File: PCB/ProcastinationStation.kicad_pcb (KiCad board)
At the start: 2 copper layers, 87 x 120 mm, 21 parts, among them J1 Conn_01x14_Socket, SW1 Up, SW10 X, SW11 L1, SW12 R2, SW13 Right, SW14 Y, SW2 A, SW3 Start, SW4 R1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

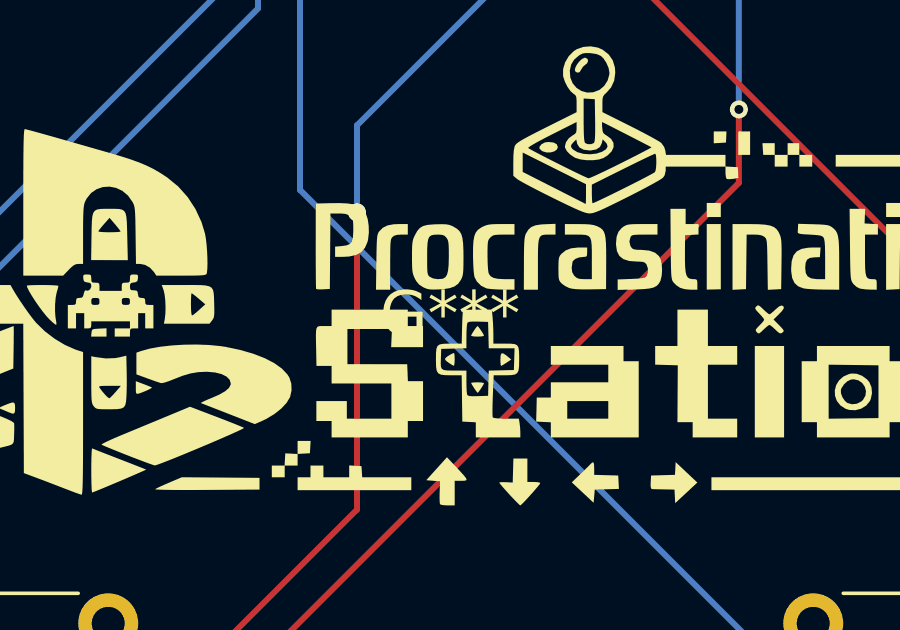
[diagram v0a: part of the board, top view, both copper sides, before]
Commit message: Update PCB schematic and layout
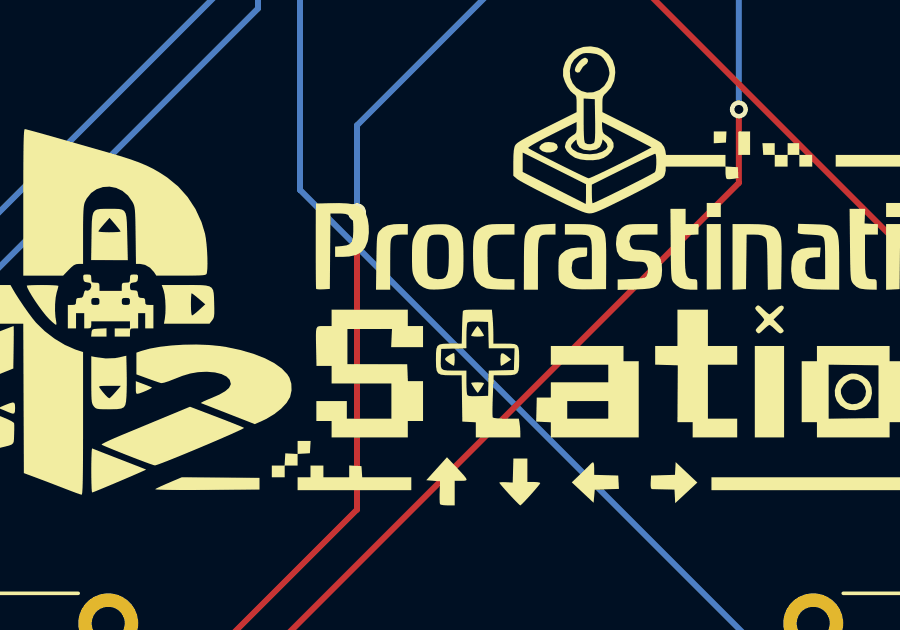
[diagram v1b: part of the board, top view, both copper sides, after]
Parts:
- added G***: LOGO, LOGO, B.Cu at (142.6, 118.0)
- renumbered TP1 to CS1, TP2 to MOSI1, TP3 to SCK1
